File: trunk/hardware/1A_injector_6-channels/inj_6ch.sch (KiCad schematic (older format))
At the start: 35 parts, among them P1 HEADER_10X2, P2 CONN_2, P3 CONN_3, P4 CONN_2, P5 CONN_3, P7 HEADER_10X2, Q1 OVP_DRIVER, Q2 OVP_DRIVER, Q3 OVP_DRIVER, Q4 OVP_DRIVER, Q5 OVP_DRIVER, Q6 OVP_DRIVER

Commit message: working with BOM
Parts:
- R1, R13, R14, R15, R16, R17, R18: mfg,mfg# VISHAY,CRCW0805100KFKEA -> Panasonic,ERJ-6GEYJ102V; vend1,vend1# digi,CRCW0805100KFKEA -> digi,P1.0KACT-ND
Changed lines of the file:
@@
 F 2 "SM0805" V 1130 600 60  0001 C CNN
 F 3 "" H 4200 2625 60  0001 C CNN
-F 4 "VISHAY,CRCW0805100KFKEA" V 1130 600 60  0001 C CNN "mfg,mfg#"
-F 5 "digi,CRCW0805100KFKEA" V 1130 600 60  0001 C CNN "vend1,vend1#"
+F 4 "Panasonic,ERJ-6GEYJ102V" V 1130 600 60  0001 C CNN "mfg,mfg#"
+F 5 "digi,P1.0KACT-ND" V 1130 600 60  0001 C CNN "vend1,vend1#"
 	1    4200 2625
 	0    1    -1   0
@@
 F 2 "SM0805" V 1130 -100 60  0001 C CNN
 F 3 "" H 4200 2275 60  0001 C CNN
-F 4 "VISHAY,CRCW0805100KFKEA" V 1130 -100 60  0001 C CNN "mfg,mfg#"
-F 5 "digi,CRCW0805100KFKEA" V 1130 -100 60  0001 C CNN "vend1,vend1#"
+F 4 "Panasonic,ERJ-6GEYJ102V" V 1130 -100 60  0001 C CNN "mfg,mfg#"
+F 5 "digi,P1.0KACT-ND" V 1130 -100 60  0001 C CNN "vend1,vend1#"
 	1    4200 2275
 	0    1    1    0
@@
 F 2 "SM0805" V 1130 3100 60  0001 C CNN
 F 3 "" H 4200 3875 60  0001 C CNN
-F 4 "VISHAY,CRCW0805100KFKEA" V 1130 3100 60  0001 C CNN "mfg,mfg#"
-F 5 "digi,CRCW0805100KFKEA" V 1130 3100 60  0001 C CNN "vend1,vend1#"
+F 4 "Panasonic,ERJ-6GEYJ102V" V 1130 3100 60  0001 C CNN "mfg,mfg#"
+F 5 "digi,P1.0KACT-ND" V 1130 3100 60  0001 C CNN "vend1,vend1#"
 	1    4200 3875
 	0    1    -1   0
@@
 F 2 "SM0805" V 1130 2400 60  0001 C CNN
 F 3 "" H 4200 3525 60  0001 C CNN
-F 4 "VISHAY,CRCW0805100KFKEA" V 1130 2400 60  0001 C CNN "mfg,mfg#"
-F 5 "digi,CRCW0805100KFKEA" V 1130 2400 60  0001 C CNN "vend1,vend1#"
+F 4 "Panasonic,ERJ-6GEYJ102V" V 1130 2400 60  0001 C CNN "mfg,mfg#"
+F 5 "digi,P1.0KACT-ND" V 1130 2400 60  0001 C CNN "vend1,vend1#"
 	1    4200 3525
 	0    1    1    0
@@
 F 2 "SM0805" V 1130 4900 60  0001 C CNN
 F 3 "" H 4200 4775 60  0001 C CNN
-F 4 "VISHAY,CRCW0805100KFKEA" V 1130 4900 60  0001 C CNN "mfg,mfg#"
-F 5 "digi,CRCW0805100KFKEA" V 1130 4900 60  0001 C CNN "vend1,vend1#"
+F 4 "Panasonic,ERJ-6GEYJ102V" V 1130 4900 60  0001 C CNN "mfg,mfg#"
+F 5 "digi,P1.0KACT-ND" V 1130 4900 60  0001 C CNN "vend1,vend1#"
 	1    4200 4775
 	0    1    1    0
@@
 F 2 "SM0805" V 1130 5600 60  0001 C CNN
 F 3 "" H 4200 5125 60  0001 C CNN
-F 4 "VISHAY,CRCW0805100KFKEA" V 1130 5600 60  0001 C CNN "mfg,mfg#"
-F 5 "digi,CRCW0805100KFKEA" V 1130 5600 60  0001 C CNN "vend1,vend1#"
+F 4 "Panasonic,ERJ-6GEYJ102V" V 1130 5600 60  0001 C CNN "mfg,mfg#"
+F 5 "digi,P1.0KACT-ND" V 1130 5600 60  0001 C CNN "vend1,vend1#"
 	1    4200 5125
 	0    1    -1   0
@@
 F 2 "SM0805" V 2080 4100 60  0001 C CNN
 F 3 "" H 5150 6475 60  0001 C CNN
-F 4 "VISHAY,CRCW0805100KFKEA" V 2080 4100 60  0001 C CNN "mfg,mfg#"
-F 5 "digi,CRCW0805100KFKEA" V 2080 4100 60  0001 C CNN "vend1,vend1#"
+F 4 "Panasonic,ERJ-6GEYJ102V" V 2080 4100 60  0001 C CNN "mfg,mfg#"
+F 5 "digi,P1.0KACT-ND" V 2080 4100 60  0001 C CNN "vend1,vend1#"
 	1    5150 6475
 	0    -1   1    0

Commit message: BOM improvements
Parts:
- P2, P4: mfg 1760490000 -> (none); mfg,mfg# (none) -> OST,OSTTC022162; vend1,vend1# (none) -> digi,ED2609-ND
- P3: mfg# 1760500000 -> (none); mfg,mfg# (none) -> OST,OSTTC032162; vend1,vend1# (none) -> digi,ED2610-ND
- P5: mfg# 1760500000 -> (none); mfg,mfg# (none) -> OST,OSTTC022162; vend1,vend1# (none) -> digi,ED2609-ND
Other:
- note added: "2 position\nterminal is\nused here"
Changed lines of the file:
@@
 Sheet 1 1
 Title "6 Channel Injector"
-Date "24 dec 2013"
+Date "30 dec 2013"
 Rev "A-6"
 Comp "http://code.google.com/p/daecu/"
@@
 F 2 "bornier3" H 5800 3625 60  0001 C CNN
 F 3 "" H 5800 3625 60  0000 C CNN
-F 4 "1760500000" V 5800 3625 60  0001 C CNN "mfg#"
+F 4 "OST,OSTTC032162" V 5800 3625 60  0001 C CNN "mfg,mfg#"
+F 5 "digi,ED2610-ND" V 5800 3625 60  0001 C CNN "vend1,vend1#"
 	1    5800 3625
 	1    0    0    1
@@
 F 2 "bornier2" H 5800 3925 60  0001 C CNN
 F 3 "" H 5800 3925 60  0000 C CNN
-F 4 "1760490000" V 5800 3925 60  0001 C CNN "mfg"
+F 4 "OST,OSTTC022162" V 5800 3925 60  0001 C CNN "mfg,mfg#"
+F 5 "digi,ED2609-ND" V 5800 3925 60  0001 C CNN "vend1,vend1#"
 	1    5800 3925
 	1    0    0    1
@@
 F 2 "bornier2" H 5800 3325 60  0001 C CNN
 F 3 "" H 5800 3325 60  0000 C CNN
-F 4 "1760490000" V 5800 3325 60  0001 C CNN "mfg"
+F 4 "OST,OSTTC022162" V 5800 3325 60  0001 C CNN "mfg,mfg#"
+F 5 "digi,ED2609-ND" V 5800 3325 60  0001 C CNN "vend1,vend1#"
 	1    5800 3325
 	1    0    0    1
@@
 F 2 "bornier3" H 725 6475 60  0001 C CNN
 F 3 "" H 725 6475 60  0000 C CNN
-F 4 "1760500000" V 725 6475 60  0001 C CNN "mfg#"
+F 4 "OST,OSTTC022162" V 725 6475 60  0001 C CNN "mfg,mfg#"
+F 5 "digi,ED2609-ND" V 725 6475 60  0001 C CNN "vend1,vend1#"
 	1    725  6475
 	-1   0    0    -1
@@
 	1    0    0    -1
 $EndComp
+Text Notes 550  6050 0    60   ~ 0
+2 position\nterminal is\nused here
 $EndSCHEMATC

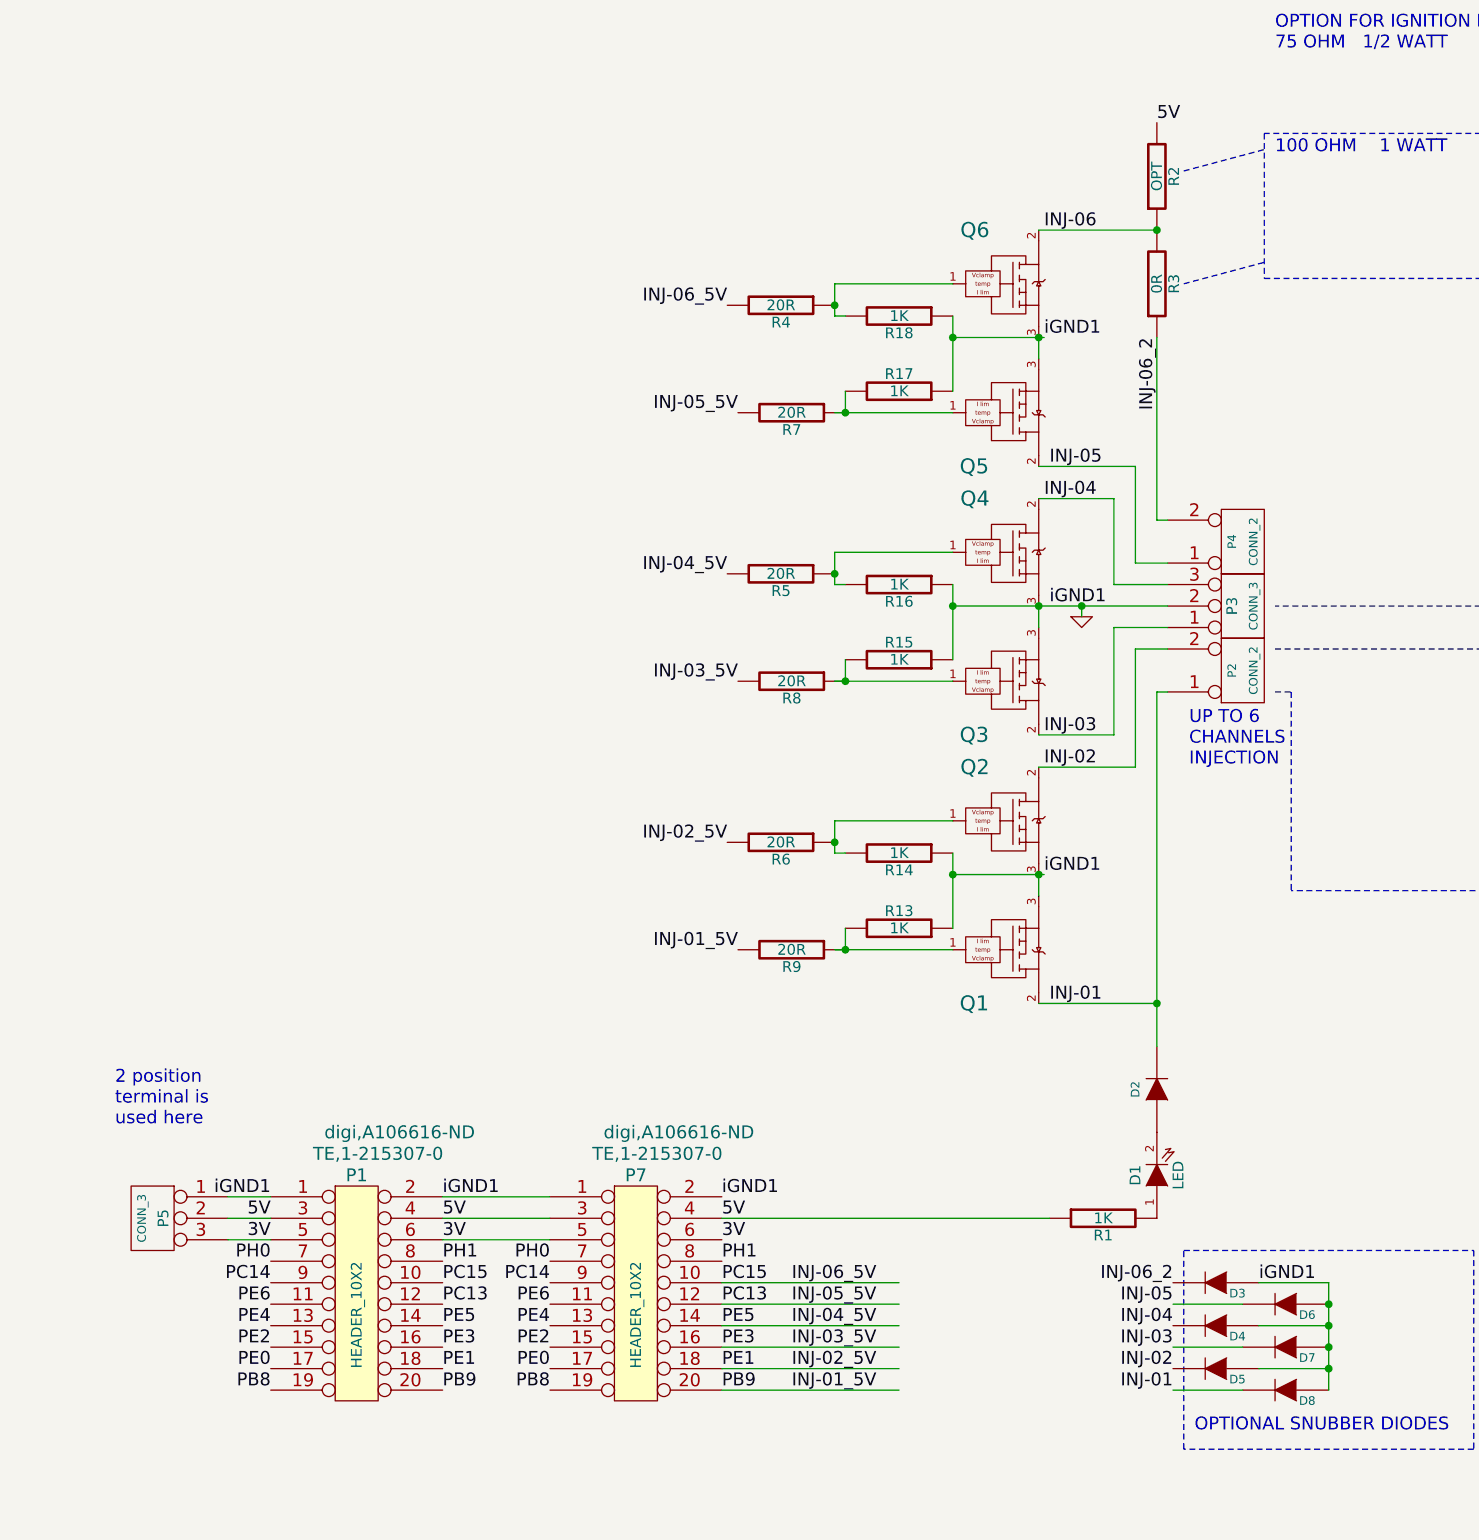
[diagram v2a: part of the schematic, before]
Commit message: better naming
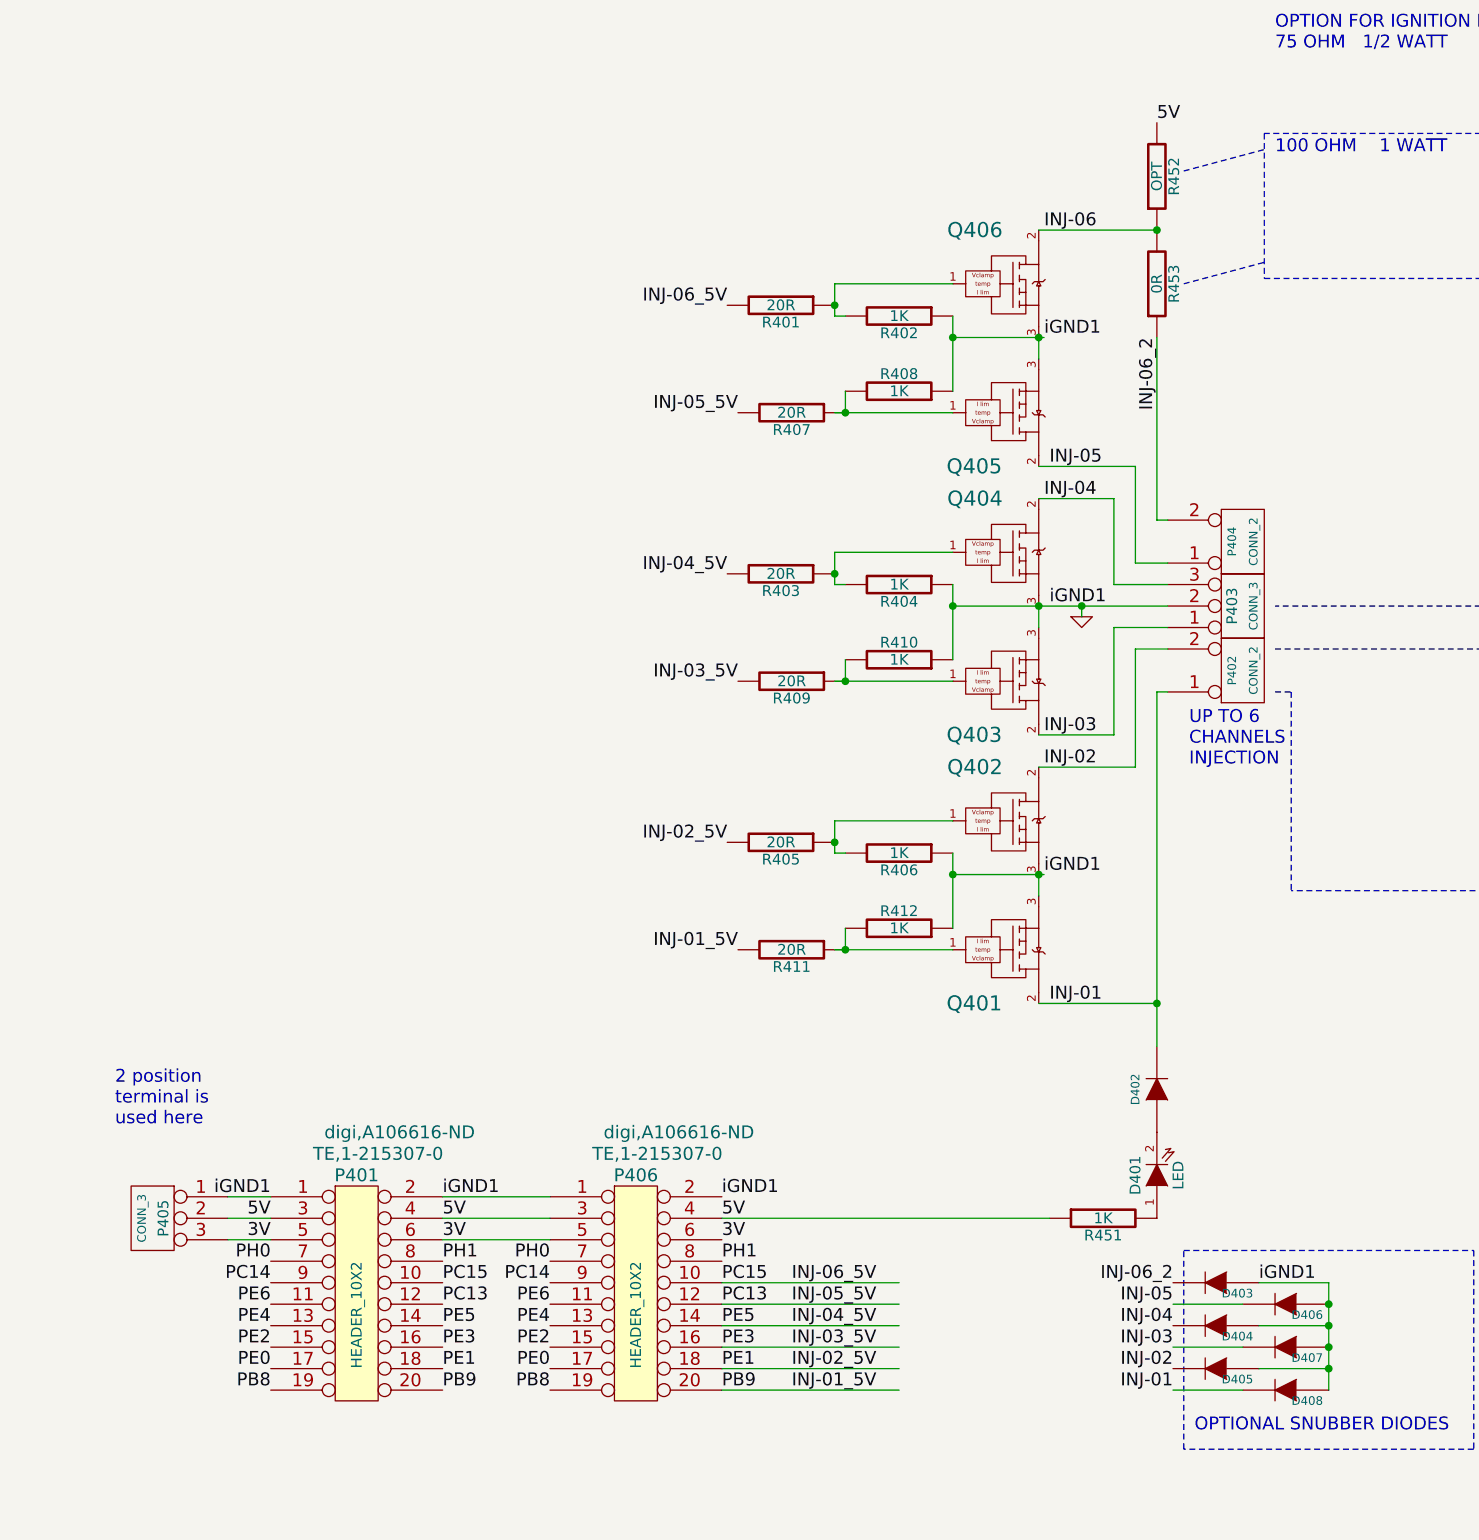
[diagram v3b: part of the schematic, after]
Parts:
- renumbered D1 to D401, D2 to D402, D3 to D403, D4 to D404, D5 to D405, D6 to D406, D7 to D407, D8 to D408, P1 to P401, P2 to P402, P3 to P403, P4 to P404, P5 to P405, P7 to P406, Q1 to Q401, Q2 to Q402, Q3 to Q403, Q4 to Q404, Q5 to Q405, Q6 to Q406, R4 to R401, R18 to R402, R5 to R403, R16 to R404, R6 to R405, R14 to R406, R7 to R407, R17 to R408, R8 to R409, R15 to R410, R9 to R411, R13 to R412, R1 to R451, R2 to R452, R3 to R453
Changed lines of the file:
@@
 BAT
 $Comp
-L FDS2734 Q6
+L FDS2734 Q406
 U 1 1 50D3B114
 P 4650 2125
-F 0 "Q6" H 4553 2375 70  0000 C CNN
+F 0 "Q406" H 4553 2375 70  0000 C CNN
 F 1 "OVP_DRIVER" H 4275 2275 60  0001 C CNN
 F 2 "SO8E_ST" V 1130 -400 60  0001 C CNN
@@
 $EndComp
 $Comp
-L FDS2734 Q5
+L FDS2734 Q405
 U 1 1 50D3B113
 P 4650 2725
-F 0 "Q5" H 4550 2975 70  0000 C CNN
+F 0 "Q405" H 4550 2975 70  0000 C CNN
 F 1 "OVP_DRIVER" H 4300 2875 60  0001 C CNN
 F 2 "SO8E_ST" V 1130 800 60  0001 C CNN
@@
 $EndComp
 $Comp
-L R R17
+L R R408
 U 1 1 50D3B111
 P 4200 2625
-F 0 "R17" V 4280 2625 50  0000 C CNN
+F 0 "R408" V 4280 2625 50  0000 C CNN
 F 1 "1K" V 4200 2625 50  0000 C CNN
 F 2 "SM0805" V 1130 600 60  0001 C CNN
@@
 INJ-06_5V
 $Comp
-L R R18
+L R R402
 U 1 1 50D3B10F
 P 4200 2275
-F 0 "R18" V 4280 2275 50  0000 C CNN
+F 0 "R402" V 4280 2275 50  0000 C CNN
 F 1 "1K" V 4200 2275 50  0000 C CNN
 F 2 "SM0805" V 1130 -100 60  0001 C CNN
@@
 INJ-06
 $Comp
-L FDS2734 Q4
+L FDS2734 Q404
 U 1 1 50D3B0FD
 P 4650 3375
-F 0 "Q4" H 4553 3625 70  0000 C CNN
+F 0 "Q404" H 4553 3625 70  0000 C CNN
 F 1 "OVP_DRIVER" H 4275 3525 60  0001 C CNN
 F 2 "SO8E_ST" V 1130 2100 60  0001 C CNN
@@
 $EndComp
 $Comp
-L FDS2734 Q3
+L FDS2734 Q403
 U 1 1 50D3B0FC
 P 4650 3975
-F 0 "Q3" H 4550 4225 70  0000 C CNN
+F 0 "Q403" H 4550 4225 70  0000 C CNN
 F 1 "OVP_DRIVER" H 4300 4125 60  0001 C CNN
 F 2 "SO8E_ST" V 1130 3300 60  0001 C CNN
@@
 $EndComp
 $Comp
-L R R15
+L R R410
 U 1 1 50D3B0FA
 P 4200 3875
-F 0 "R15" V 4280 3875 50  0000 C CNN
+F 0 "R410" V 4280 3875 50  0000 C CNN
 F 1 "1K" V 4200 3875 50  0000 C CNN
 F 2 "SM0805" V 1130 3100 60  0001 C CNN
@@
 INJ-04_5V
 $Comp
-L R R16
+L R R404
 U 1 1 50D3B0F8
 P 4200 3525
-F 0 "R16" V 4280 3525 50  0000 C CNN
+F 0 "R404" V 4280 3525 50  0000 C CNN
 F 1 "1K" V 4200 3525 50  0000 C CNN
 F 2 "SM0805" V 1130 2400 60  0001 C CNN
@@
 INJ-01
 $Comp
-L R R14
+L R R406
 U 1 1 50D3AF9A
 P 4200 4775
-F 0 "R14" V 4280 4775 50  0000 C CNN
+F 0 "R406" V 4280 4775 50  0000 C CNN
 F 1 "1K" V 4200 4775 50  0000 C CNN
 F 2 "SM0805" V 1130 4900 60  0001 C CNN
@@
 iGND1
 $Comp
-L R R13
+L R R412
 U 1 1 50D3AF94
 P 4200 5125
-F 0 "R13" V 4280 5125 50  0000 C CNN
+F 0 "R412" V 4280 5125 50  0000 C CNN
 F 1 "1K" V 4200 5125 50  0000 C CNN
 F 2 "SM0805" V 1130 5600 60  0001 C CNN
@@
 FUSE
 $Comp
-L FDS2734 Q1
+L FDS2734 Q401
 U 1 1 4E3ED60F
 P 4650 5225
-F 0 "Q1" H 4550 5475 70  0000 C CNN
+F 0 "Q401" H 4550 5475 70  0000 C CNN
 F 1 "OVP_DRIVER" H 4300 5375 60  0001 C CNN
 F 2 "SO8E_ST" V 1130 5800 60  0001 C CNN
@@
 $EndComp
 $Comp
-L FDS2734 Q2
+L FDS2734 Q402
 U 1 1 4E3ED60B
 P 4650 4625
-F 0 "Q2" H 4553 4875 70  0000 C CNN
+F 0 "Q402" H 4553 4875 70  0000 C CNN
 F 1 "OVP_DRIVER" H 4275 4775 60  0001 C CNN
 F 2 "SO8E_ST" V 1130 4600 60  0001 C CNN
@@
 	9350 3425 8025 3425
 $Comp
-L CONN_3 P3
+L CONN_3 P403
 U 1 1 527D6DAD
 P 5800 3625
-F 0 "P3" V 5750 3625 50  0000 C CNN
+F 0 "P403" V 5750 3625 50  0000 C CNN
 F 1 "CONN_3" V 5850 3625 40  0000 C CNN
 F 2 "bornier3" H 5800 3625 60  0001 C CNN
@@
 $EndComp
 $Comp
-L CONN_2 P2
+L CONN_2 P402
 U 1 1 527D7F53
 P 5800 3925
-F 0 "P2" V 5750 3925 40  0000 C CNN
+F 0 "P402" V 5750 3925 40  0000 C CNN
 F 1 "CONN_2" V 5850 3925 40  0000 C CNN
 F 2 "bornier2" H 5800 3925 60  0001 C CNN
@@
 iGND1
 $Comp
-L CONN_2 P4
+L CONN_2 P404
 U 1 1 527D96A0
 P 5800 3325
-F 0 "P4" V 5750 3325 40  0000 C CNN
+F 0 "P404" V 5750 3325 40  0000 C CNN
 F 1 "CONN_2" V 5850 3325 40  0000 C CNN
 F 2 "bornier2" H 5800 3325 60  0001 C CNN
@@
 PH1
 $Comp
-L CONN_3 P5
+L CONN_3 P405
 U 1 1 527E234B
 P 725 6475
-F 0 "P5" V 675 6475 50  0000 C CNN
+F 0 "P405" V 675 6475 50  0000 C CNN
 F 1 "CONN_3" V 775 6475 40  0000 C CNN
 F 2 "bornier3" H 725 6475 60  0001 C CNN
@@
 	2075 6575 2575 6575
 $Comp
-L LED D1
+L LED D401
 U 1 1 527FB778
 P 5400 6275
-F 0 "D1" H 5400 6375 50  0000 C CNN
+F 0 "D401" H 5400 6375 50  0000 C CNN
 F 1 "LED" H 5400 6175 50  0000 C CNN
 F 2 "LED-0805" H 5400 6275 60  0001 C CNN
@@
 $EndComp
 $Comp
-L DIODE D2
+L DIODE D402
 U 1 1 527FB789
 P 5400 5875
-F 0 "D2" H 5400 5975 40  0000 C CNN
+F 0 "D402" H 5400 5975 40  0000 C CNN
 F 1 "DIODE" H 5400 5775 40  0001 C CNN
 F 2 "SOD-123" H 5400 5875 60  0001 C CNN
@@
 $EndComp
 $Comp
-L R R1
+L R R451
 U 1 1 527FB7A2
 P 5150 6475
-F 0 "R1" V 5230 6475 50  0000 C CNN
+F 0 "R451" V 5230 6475 50  0000 C CNN
 F 1 "1K" V 5150 6475 50  0000 C CNN
 F 2 "SM0805" V 2080 4100 60  0001 C CNN
@@
 	4900 6475 3375 6475
 $Comp
-L DIODE D3
+L DIODE D403
 U 1 1 527FF3F6
 P 5675 6775
-F 0 "D3" H 5575 6825 40  0000 C CNN
+F 0 "D403" H 5575 6825 40  0000 C CNN
 F 1 "DIODE" H 5675 6675 40  0001 C CNN
 F 2 "SIL-2" H 5675 6775 60  0001 C CNN
@@
 $EndComp
 $Comp
-L DIODE D6
+L DIODE D406
 U 1 1 527FF563
 P 6000 6875
-F 0 "D6" H 5900 6925 40  0000 C CNN
+F 0 "D406" H 5900 6925 40  0000 C CNN
 F 1 "DIODE" H 6000 6775 40  0001 C CNN
 F 2 "SIL-2" H 6000 6875 60  0001 C CNN
@@
 $EndComp
 $Comp
-L DIODE D4
+L DIODE D404
 U 1 1 527FF56A
 P 5675 6975
-F 0 "D4" H 5575 7025 40  0000 C CNN
+F 0 "D404" H 5575 7025 40  0000 C CNN
 F 1 "DIODE" H 5675 6875 40  0001 C CNN
 F 2 "SIL-2" H 5675 6975 60  0001 C CNN
@@
 $EndComp
 $Comp
-L DIODE D7
+L DIODE D407
 U 1 1 527FF571
 P 6000 7075
-F 0 "D7" H 5900 7125 40  0000 C CNN
+F 0 "D407" H 5900 7125 40  0000 C CNN
 F 1 "DIODE" H 6000 6975 40  0001 C CNN
 F 2 "SIL-2" H 6000 7075 60  0001 C CNN
@@
 $EndComp
 $Comp
-L DIODE D5
+L DIODE D405
 U 1 1 527FF578
 P 5675 7175
-F 0 "D5" H 5575 7225 40  0000 C CNN
+F 0 "D405" H 5575 7225 40  0000 C CNN
 F 1 "DIODE" H 5675 7075 40  0001 C CNN
 F 2 "SIL-2" H 5675 7175 60  0001 C CNN
@@
 $EndComp
 $Comp
-L DIODE D8
+L DIODE D408
 U 1 1 527FF57F
 P 6000 7275
-F 0 "D8" H 5900 7325 40  0000 C CNN
+F 0 "D408" H 5900 7325 40  0000 C CNN
 F 1 "DIODE" H 6000 7175 40  0001 C CNN
 F 2 "SIL-2" H 6000 7275 60  0001 C CNN
@@
 	6875 6625 6875 7550
 $Comp
-L R R2
+L R R452
 U 1 1 527FFC06
 P 5400 1625
-F 0 "R2" V 5480 1625 50  0000 C CNN
+F 0 "R452" V 5480 1625 50  0000 C CNN
 F 1 "OPT" V 5400 1625 50  0000 C CNN
 F 2 "SIL-2" V 2330 -750 60  0001 C CNN
@@
 $EndComp
 $Comp
-L R R3
+L R R453
 U 1 1 527FFC31
 P 5400 2125
-F 0 "R3" V 5480 2125 50  0000 C CNN
+F 0 "R453" V 5480 2125 50  0000 C CNN
 F 1 "0R" V 5400 2125 50  0000 C CNN
 F 2 "SIL-2" V 2330 -250 60  0001 C CNN
@@
 INJ-06_2
 $Comp
-L R R4
+L R R401
 U 1 1 529A8640
 P 3650 2225
-F 0 "R4" V 3730 2225 50  0000 C CNN
+F 0 "R401" V 3730 2225 50  0000 C CNN
 F 1 "20R" V 3650 2225 50  0000 C CNN
 F 2 "SM0805" V 580 -150 60  0001 C CNN
@@
 	3900 2125 4450 2125
 $Comp
-L R R7
+L R R407
 U 1 1 529A8879
 P 3700 2725
-F 0 "R7" V 3780 2725 50  0000 C CNN
+F 0 "R407" V 3780 2725 50  0000 C CNN
 F 1 "20R" V 3700 2725 50  0000 C CNN
 F 2 "SM0805" V 630 350 60  0001 C CNN
@@
 $EndComp
 $Comp
-L R R5
+L R R403
 U 1 1 529A8883
 P 3650 3475
-F 0 "R5" V 3730 3475 50  0000 C CNN
+F 0 "R403" V 3730 3475 50  0000 C CNN
 F 1 "20R" V 3650 3475 50  0000 C CNN
 F 2 "SM0805" V 580 1100 60  0001 C CNN
@@
 $EndComp
 $Comp
-L R R8
+L R R409
 U 1 1 529A888D
 P 3700 3975
-F 0 "R8" V 3780 3975 50  0000 C CNN
+F 0 "R409" V 3780 3975 50  0000 C CNN
 F 1 "20R" V 3700 3975 50  0000 C CNN
 F 2 "SM0805" V 630 1600 60  0001 C CNN
@@
 $EndComp
 $Comp
-L R R6
+L R R405
 U 1 1 529A8899
 P 3650 4725
-F 0 "R6" V 3730 4725 50  0000 C CNN
+F 0 "R405" V 3730 4725 50  0000 C CNN
 F 1 "20R" V 3650 4725 50  0000 C CNN
 F 2 "SM0805" V 580 2350 60  0001 C CNN
@@
 $EndComp
 $Comp
-L R R9
+L R R411
 U 1 1 529A88A3
 P 3700 5225
-F 0 "R9" V 3780 5225 50  0000 C CNN
+F 0 "R411" V 3780 5225 50  0000 C CNN
 F 1 "20R" V 3700 5225 50  0000 C CNN
 F 2 "SM0805" V 630 2850 60  0001 C CNN
@@
 $EndComp
 $Comp
-L HEADER_10X2 P1
+L HEADER_10X2 P401
 U 1 1 52B99314
 P 1675 6825
-F 0 "P1" H 1675 7375 60  0000 C CNN
+F 0 "P401" H 1675 7375 60  0000 C CNN
 F 1 "HEADER_10X2" V 1675 6725 50  0000 C CNN
 F 2 "~" H 1675 6825 60  0000 C CNN
@@
 $EndComp
 $Comp
-L HEADER_10X2 P7
+L HEADER_10X2 P406
 U 1 1 52B99443
 P 2975 6825
-F 0 "P7" H 2975 7375 60  0000 C CNN
+F 0 "P406" H 2975 7375 60  0000 C CNN
 F 1 "HEADER_10X2" V 2975 6725 50  0000 C CNN
 F 2 "~" H 2975 6825 60  0000 C CNN
